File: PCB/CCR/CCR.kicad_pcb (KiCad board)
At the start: 2 copper layers, 94.6 x 46.7 mm, 8 parts, among them SW1 SW_Left, SW2 SW_Up, SW3 SW_Right, U1 ATmega328P-A, U10 COM-09032, U3 NRF24L01_Breakout, U4 MPU-6050

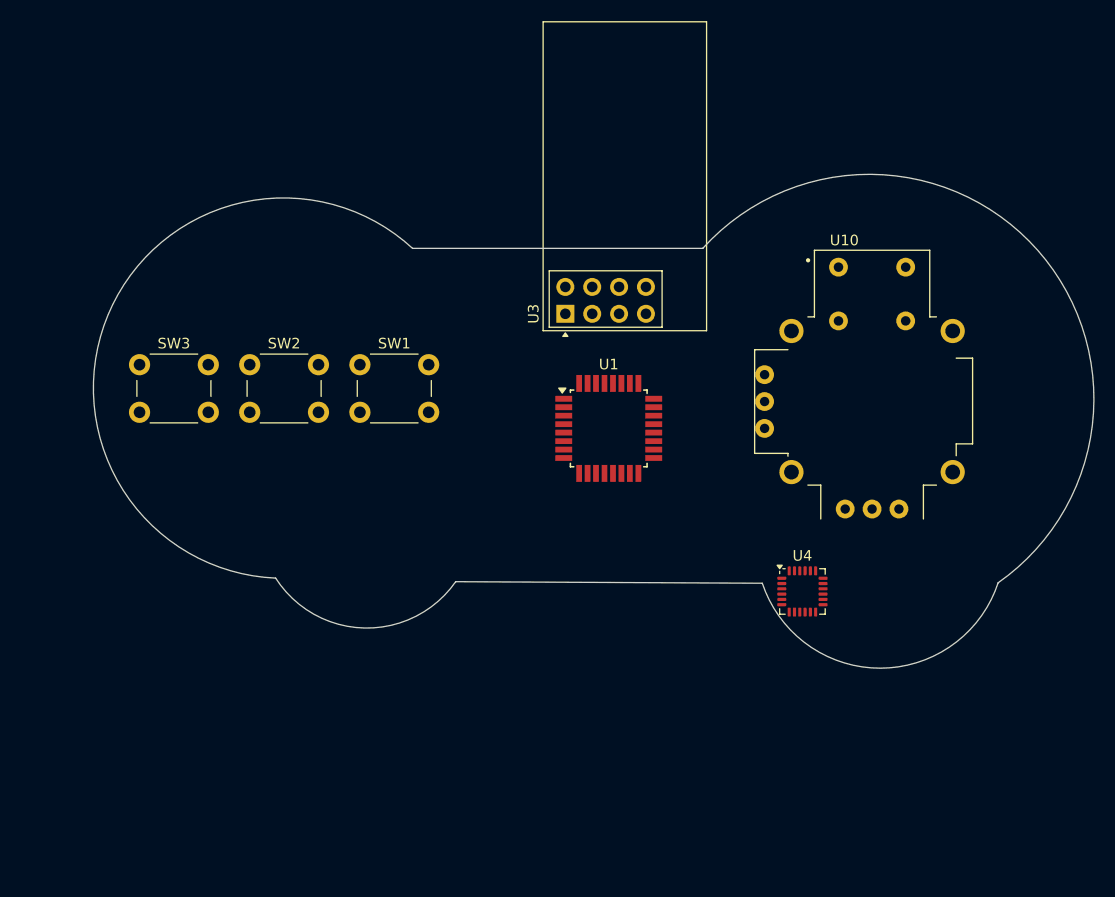
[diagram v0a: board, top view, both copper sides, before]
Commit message: Update of BME and OLED
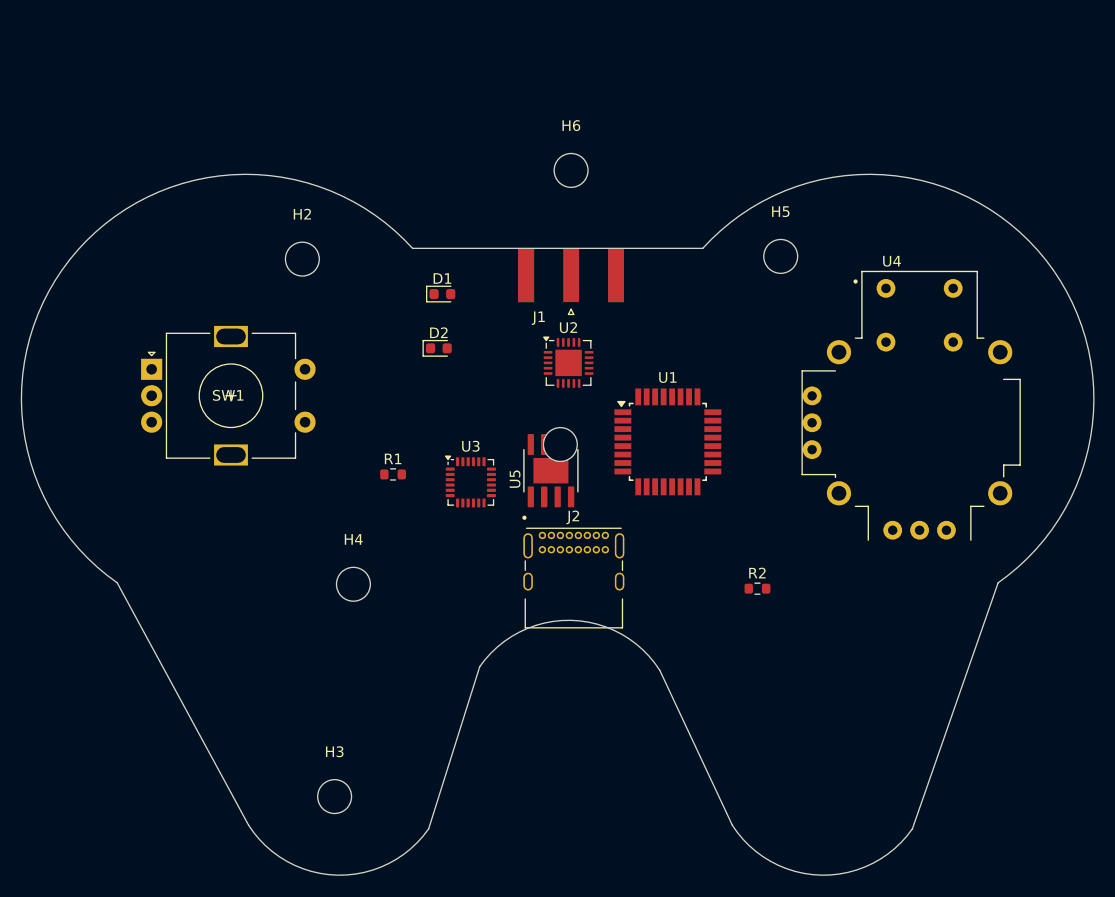
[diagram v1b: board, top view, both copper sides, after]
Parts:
- removed SW2: SW_Up, Button_Switch_THT:SW_PUSH_6mm
- removed SW3: SW_Right, Button_Switch_THT:SW_PUSH_6mm
- removed U10: COM-09032, CREPP_Joysticks:XDCR_COM-09032
- added D1: LED, LED_SMD:LED_0603_1608Metric, F.Cu at (192.3, 105.2)
- added D2: LED, LED_SMD:LED_0603_1608Metric, F.Cu at (192.0, 110.3)
- added H1: MountingHole, MountingHole:MountingHole_3.2mm_M3, B.Cu at (203.5, 119.4)
- added H2: MountingHole, MountingHole:MountingHole_3.2mm_M3, F.Cu at (179.1, 101.9)
- added H3: MountingHole, MountingHole:MountingHole_3.2mm_M3, F.Cu at (182.1, 152.7)
- added H4: MountingHole, MountingHole:MountingHole_3.2mm_M3, F.Cu at (183.9, 132.6)
- added H5: MountingHole, MountingHole:MountingHole_3.2mm_M3, F.Cu at (224.3, 101.6)
- added H6: MountingHole, MountingHole:MountingHole_3.2mm_M3, F.Cu at (204.5, 93.5)
- added J1: Connecteur_SMA, CREPP_SMA:SMA_Amphenol_132289_EdgeMount, F.Cu at (204.5, 103.4)
- added J2: USB_C_Receptacle, CREPP_Connectors_USB:USB_C_Receptacle_GCT_USB4085, F.Cu at (201.8, 128.0)
- added OLED1: ~, CREPP_Screens:SSD1306_OLED_Display_VIRTUAL_128_64, F.Cu at (204.5, 108.0)
- added R1: 270, Resistor_SMD:R_0603_1608Metric, F.Cu at (187.6, 122.2)
- added R2: 270, Resistor_SMD:R_0603_1608Metric, F.Cu at (222.1, 133.0)
- added U2: NRF24L01, Package_DFN_QFN:QFN-20-1EP_4x4mm_P0.5mm_EP2.5x2.5mm, F.Cu at (204.2, 111.7)
- added U5: TP4056, CREPP_BMS:SOP127P600X175-9N, F.Cu at (202.6, 121.9)
- SW1: value SW_Left -> RotaryEncoder_Switch; footprint Button_Switch_THT:SW_PUSH_6mm -> CREPP_RotaryEncoders:RotaryEncoder
- U3: value NRF24L01_Breakout -> MPU-6050; footprint RF_Module:nRF24L01_Breakout -> Sensor_Motion:InvenSense_QFN-24_4x4mm_P0.5mm
- U4: value MPU-6050 -> COM-09032; footprint Sensor_Motion:InvenSense_QFN-24_4x4mm_P0.5mm -> CREPP_Joysticks_SW:XDCR_COM-09032
- moved SW1 19.7 mm to (164.8, 112.3)
- moved U4 19.4 mm to (237.4, 117.3)
- moved U3 18.3 mm to (195.0, 123.0), turned to 0 degrees
- moved U1 5.73 mm to (213.6, 119.1)
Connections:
- U3 pad 1: /NRF24/GND -> unconnected-(U3-CLKIN-Pad1)
- U3 pad 2: /NRF24/+3.3V -> unconnected-(U3-NC-Pad2)
- U3 pad 3: /NRF24/CE -> unconnected-(U3-NC-Pad3)
- U3 pad 4: /NRF24/~{CSN} -> unconnected-(U3-NC-Pad4)
- U3 pad 5: /NRF24/SCK -> unconnected-(U3-NC-Pad5)
- U3 pad 6: /NRF24/MOSI -> unconnected-(U3-AUX_DA-Pad6)
- U3 pad 7: /NRF24/MISO -> unconnected-(U3-AUX_CL-Pad7)
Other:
- board size 94.6 x 46.7 mm -> 101.4 x 66.2 mm
